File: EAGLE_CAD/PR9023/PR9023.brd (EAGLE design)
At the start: 70 x 70 mm, 72 parts, among them SW1 ESWT_TL3315

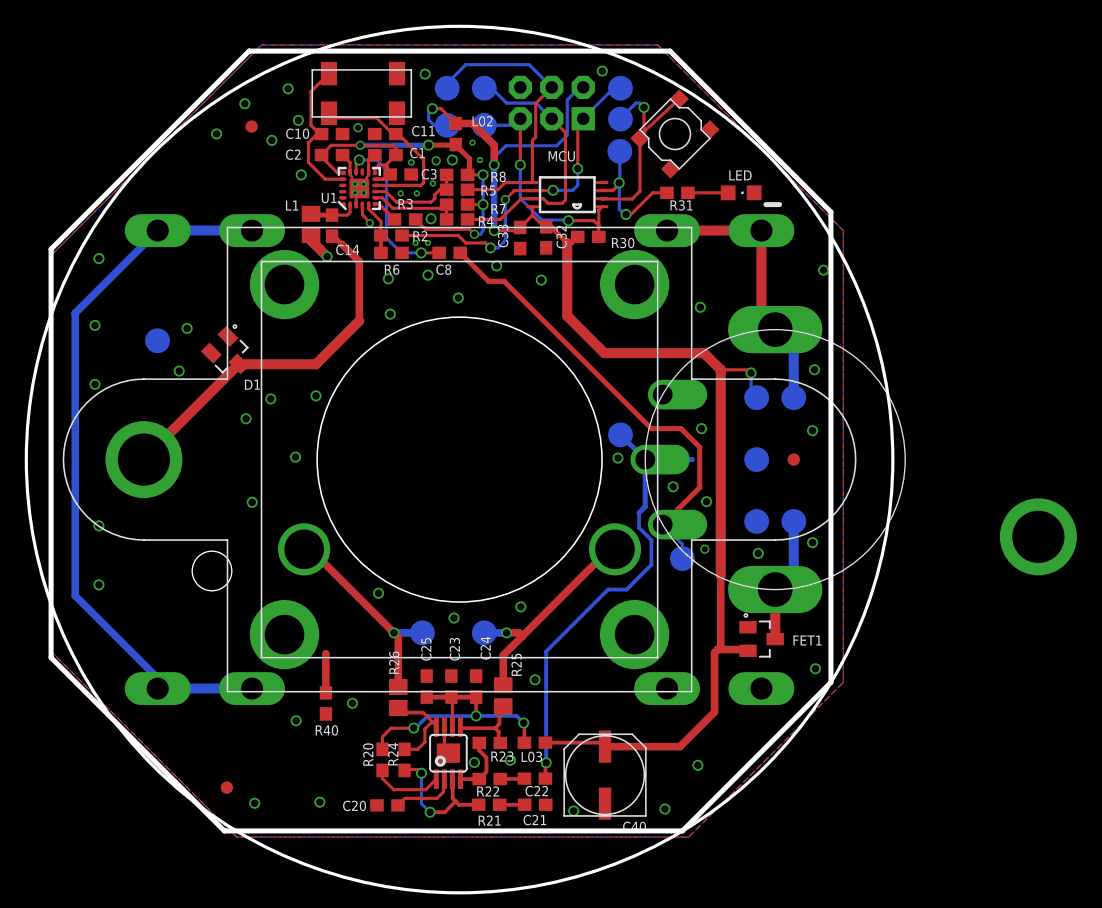
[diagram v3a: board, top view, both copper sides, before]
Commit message: Small changes
Added ground to the speaker/lid connection
Modified board outline
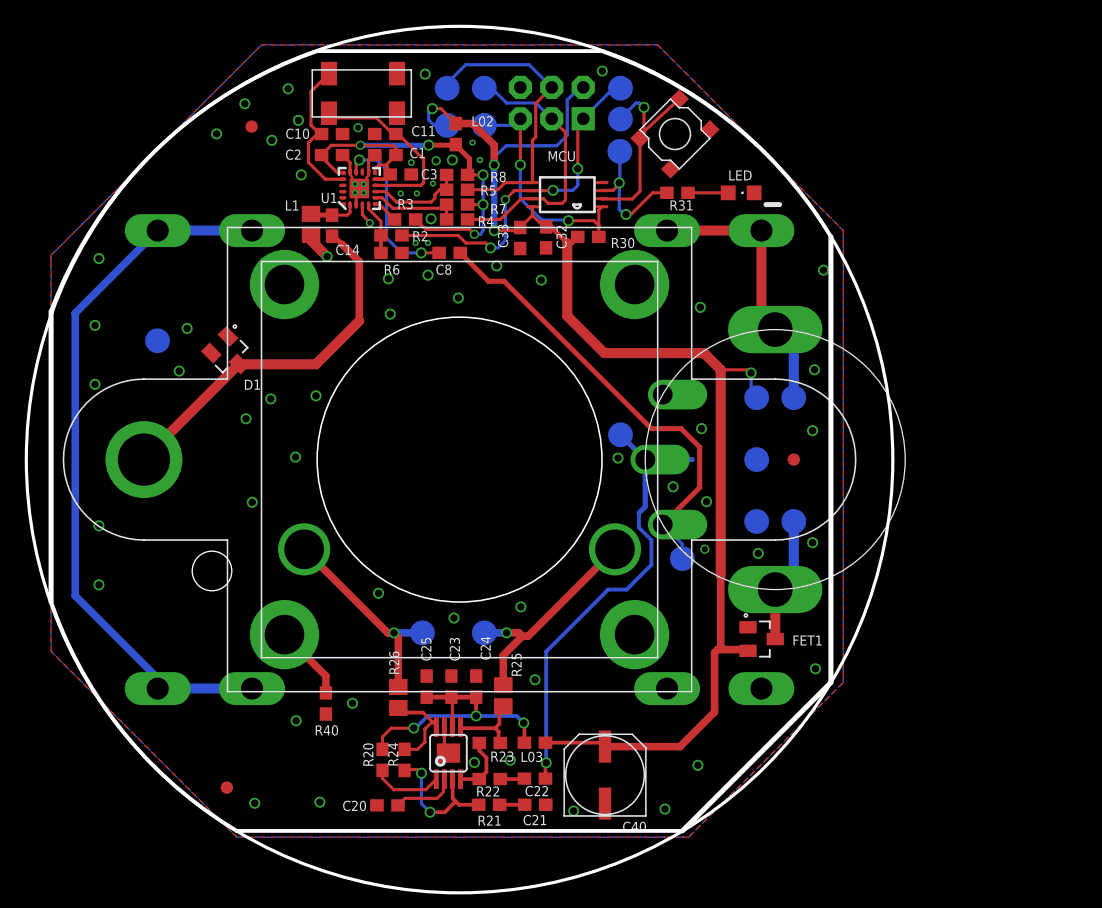
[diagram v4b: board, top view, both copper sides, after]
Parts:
- removed U$5: PEM_M3_W/PIN, PR_Parts_Library:PEM_M3_NOKEEPAWAY
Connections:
- net N$6: now also SPKR_PLACE.P$4; no longer U$5.P$2
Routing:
- net N$6: track 3.17 -> 6.09 mm
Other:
- outline, holes or cut-outs redrawn
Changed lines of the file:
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@@
 <?xml version="1.0" encoding="utf-8"?>
 <!DOCTYPE eagle SYSTEM "eagle.dtd">
-<eagle version="7.5.0">
+<eagle version="6.6.0">
 <drawing>
 <settings>
@@
 <circle x="46.34" y="60.76" radius="0.5" width="0.8128" layer="26"/>
 <wire x1="59.75" y1="55.6" x2="60.85" y2="55.6" width="0.4064" layer="21"/>
-<wire x1="2" y1="19" x2="2" y2="52" width="0.4064" layer="20"/>
-<wire x1="18" y1="68" x2="52" y2="68" width="0.4064" layer="20"/>
-<wire x1="16" y1="5" x2="53" y2="5" width="0.4064" layer="20"/>
-<wire x1="65" y1="17" x2="65" y2="55" width="0.4064" layer="20"/>
+<wire x1="2" y1="23.5" x2="2" y2="47" width="0.4064" layer="20"/>
+<wire x1="23.5" y1="68" x2="46.5" y2="68" width="0.3048" layer="20"/>
+<wire x1="17" y1="5" x2="53" y2="5" width="0.3048" layer="20"/>
+<wire x1="65" y1="17" x2="65" y2="53" width="0.4064" layer="20"/>
 <circle x="35" y="35" radius="35" width="0.254" layer="20"/>
-<wire x1="2" y1="19" x2="16" y2="5" width="0.4064" layer="20"/>
 <wire x1="53" y1="5" x2="65" y2="17" width="0.4064" layer="20"/>
-<wire x1="2" y1="52" x2="18" y2="68" width="0.4064" layer="20"/>
-<wire x1="65" y1="55" x2="52" y2="68" width="0.4064" layer="20"/>
+<wire x1="2" y1="47" x2="23.5" y2="68" width="0.3048" layer="20" curve="-50.798865"/>
+<wire x1="46.5" y1="68" x2="65" y2="53" width="0.3048" layer="20" curve="-39.646795"/>
+<wire x1="17" y1="5" x2="2" y2="23.5" width="0.3048" layer="20" curve="-39.823572"/>
 </plain>
 <attributes>
@@
 <pass name="Default">
 <param name="RoutingGrid" value="50mil"/>
-<param name="AutoGrid" value="1"/>
-<param name="Efforts" value="0"/>
-<param name="TopRouterVariant" value="1"/>
 <param name="tpViaShape" value="round"/>
 <param name="PrefDir.1" value="|"/>
@@
 <attribute name="VALUE" x="32.336" y="14.891" size="1.27" layer="27" rot="R90"/>
 </element>
-<element name="U$5" library="PR_Parts_Library" package="PEM_M3_NOKEEPAWAY" value="PEM_M3_W/PIN" x="81.76" y="28.76"/>
 </elements>
 <signals>
@@
 <wire x1="38.8" y1="21" x2="39.8" y2="21" width="0.6096" layer="1"/>
 <wire x1="39.8" y1="21" x2="40.07" y2="20.73" width="0.6096" layer="1"/>
+<wire x1="38.53" y1="16.77" x2="38.53" y2="19.19" width="0.6096" layer="1"/>
 <contactref element="SPKR_PLACE" pad="P$6"/>
-<wire x1="38.53" y1="16.77" x2="38.53" y2="19.19" width="0.6096" layer="1"/>
-<wire x1="40.07" y1="20.73" x2="47.091" y2="27.751" width="0.6096" layer="1"/>
-<wire x1="47.091" y1="27.751" x2="47.556" y2="27.751" width="0.6096" layer="1"/>
+<wire x1="47.556" y1="27.751" x2="40.535" y2="20.73" width="0.6096" layer="1"/>
+<wire x1="40.535" y1="20.73" x2="40.07" y2="20.73" width="0.6096" layer="1"/>
 </signal>
 <signal name="SPK_OUT-">
@@
 <wire x1="32" y1="21" x2="29.7" y2="21" width="0.6096" layer="16"/>
 <via x="29.7" y="21" extent="1-16" drill="0.6"/>
-<contactref element="SPKR_PLACE" pad="P$5"/>
 <wire x1="30.05" y1="16.63" x2="30.05" y2="20.65" width="0.6096" layer="1"/>
 <wire x1="30.05" y1="20.65" x2="29.7" y2="21" width="0.6096" layer="1"/>
-<wire x1="29.7" y1="21" x2="22.949" y2="27.751" width="0.6096" layer="1"/>
-<wire x1="22.949" y1="27.751" x2="22.444" y2="27.751" width="0.6096" layer="1"/>
+<contactref element="SPKR_PLACE" pad="P$5"/>
+<wire x1="22.444" y1="27.751" x2="29.195" y2="21" width="0.6096" layer="1"/>
+<wire x1="29.195" y1="21" x2="29.7" y2="21" width="0.6096" layer="1"/>
 </signal>
 <signal name="N$9">
@@
 </signal>
 <signal name="N$6">
+<contactref element="SPKR_PLACE" pad="P$4"/>
 <contactref element="R40" pad="1"/>
-<contactref element="U$5" pad="P$2"/>
-<wire x1="24.2" y1="16.15" x2="24.2" y2="19.32" width="0.6096" layer="1"/>
-<wire x1="24.2" y1="19.32" x2="81.76" y2="28.76" width="0" layer="19" extent="1-1"/>
+<wire x1="24.2" y1="16.15" x2="24.2" y2="17.516" width="0.6096" layer="1"/>
+<wire x1="24.2" y1="17.516" x2="20.858" y2="20.858" width="0.6096" layer="1"/>
 </signal>
 </signals>
